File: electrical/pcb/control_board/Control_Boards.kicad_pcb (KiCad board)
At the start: 2 copper layers, 111 parts, among them J1 XT30-M, J10 Molex_172675-0613, J11 Molex_172675-0613, J12 TSW-104-07-F-T, J13 Molex_172675-0613, J14 Molex_172675-0613, J15 TSW-104-07-F-T, J16 ED2627-ND, J17 ED2627-ND, J18 ED2627-ND, J19 TSW-104-07-F-T, J2 XT30-F, J20 PEC08SAAN, J21 PPTC102LFBN-RC, J22 S9175-ND_rpi_breakout, J23 S9175-ND_rpi_breakout, J24 6posheader, J25 SSW-104-01-F-T, J26 PEC10DAAN, J27 PPTC021LFBN-RC, J28 PPTC021LFBN-RC, J29 PPTC021LFBN-RC, J3 XT30-F, J4 XT30-F, J5 XT30-M, J6 ED2580-ND, J7 TSW-104-07-F-T, J8 Molex_172675-0613, J9 Molex_172675-0613, M1 Mounting_Holes, Q1 2N3906, Q2 2N3906, Q3 2N3906, SW1 CT206124-ND, T1 test_point, T2 test_point, T3 test_point, T4 test_point, T5 test_point, T6 test_point, U1 INA260, U2 PCA9685, U3 D24V22Fx, U4 D24V150Fx, U5 DC7G3HWA, U6 DC7G3HWA, y1 rover_silkscreen

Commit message: Adding edge cuts to control boards
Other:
- board outline added: 181.6 x 252.8 mm

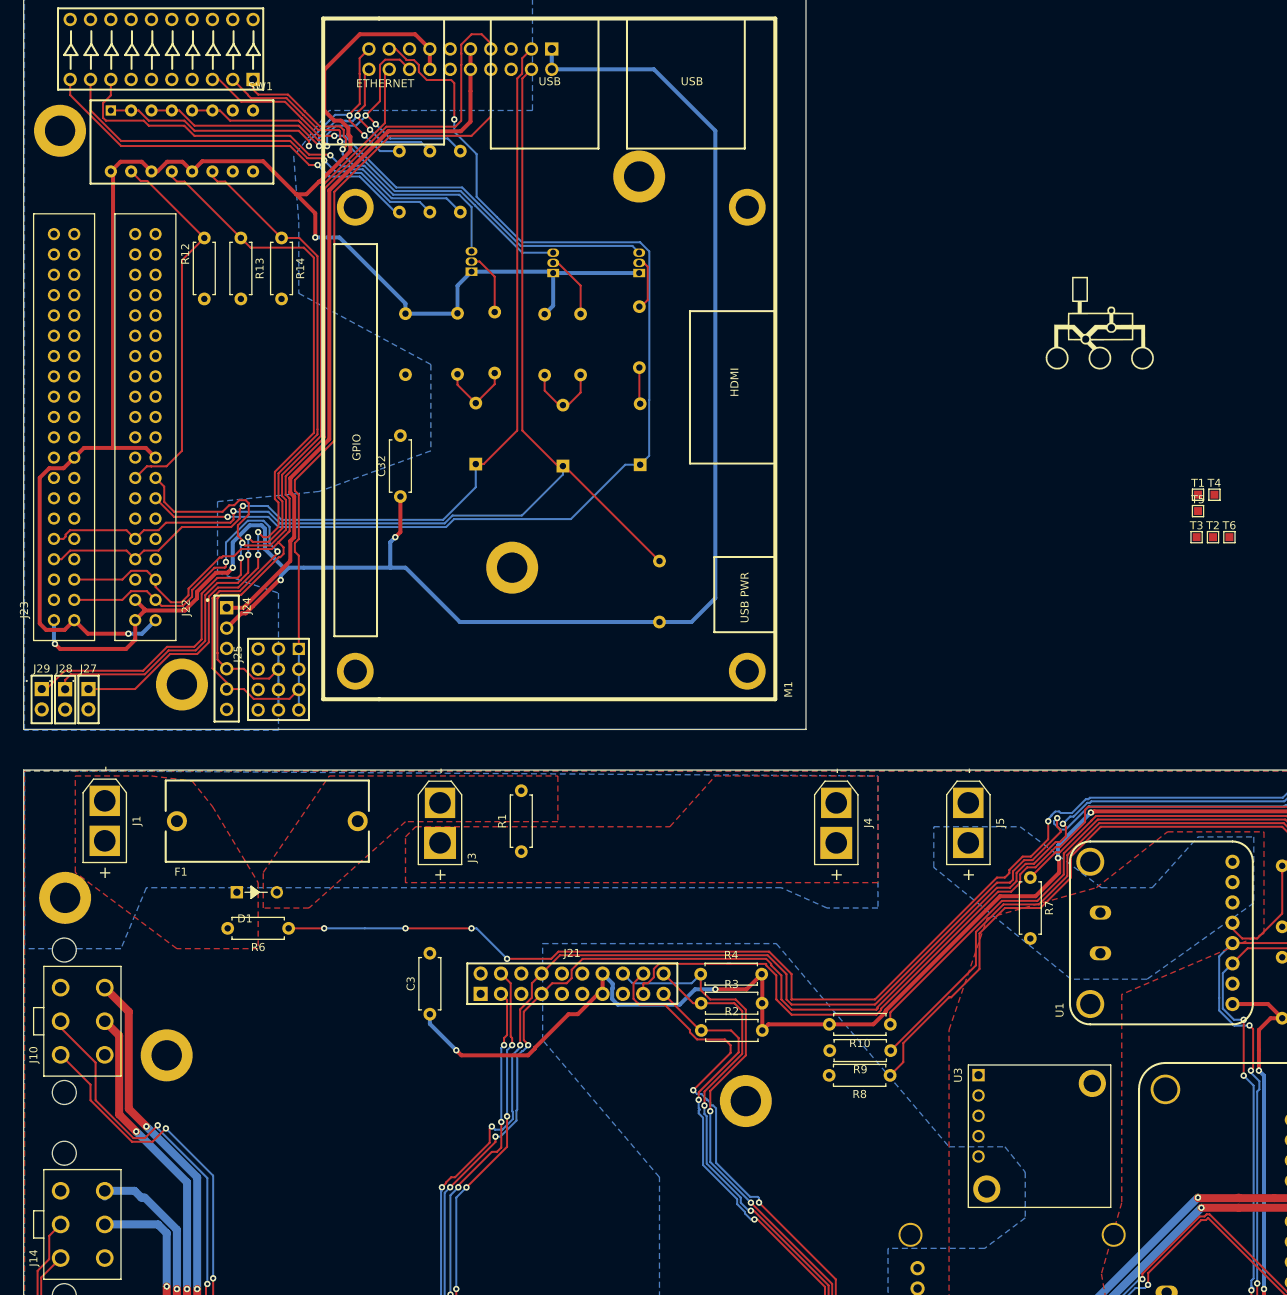
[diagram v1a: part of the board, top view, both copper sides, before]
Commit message: Updates to layout
- Placed 12V_enable line in layout
- Placed additional LED resistors in layout
- Placed testpoints in layout
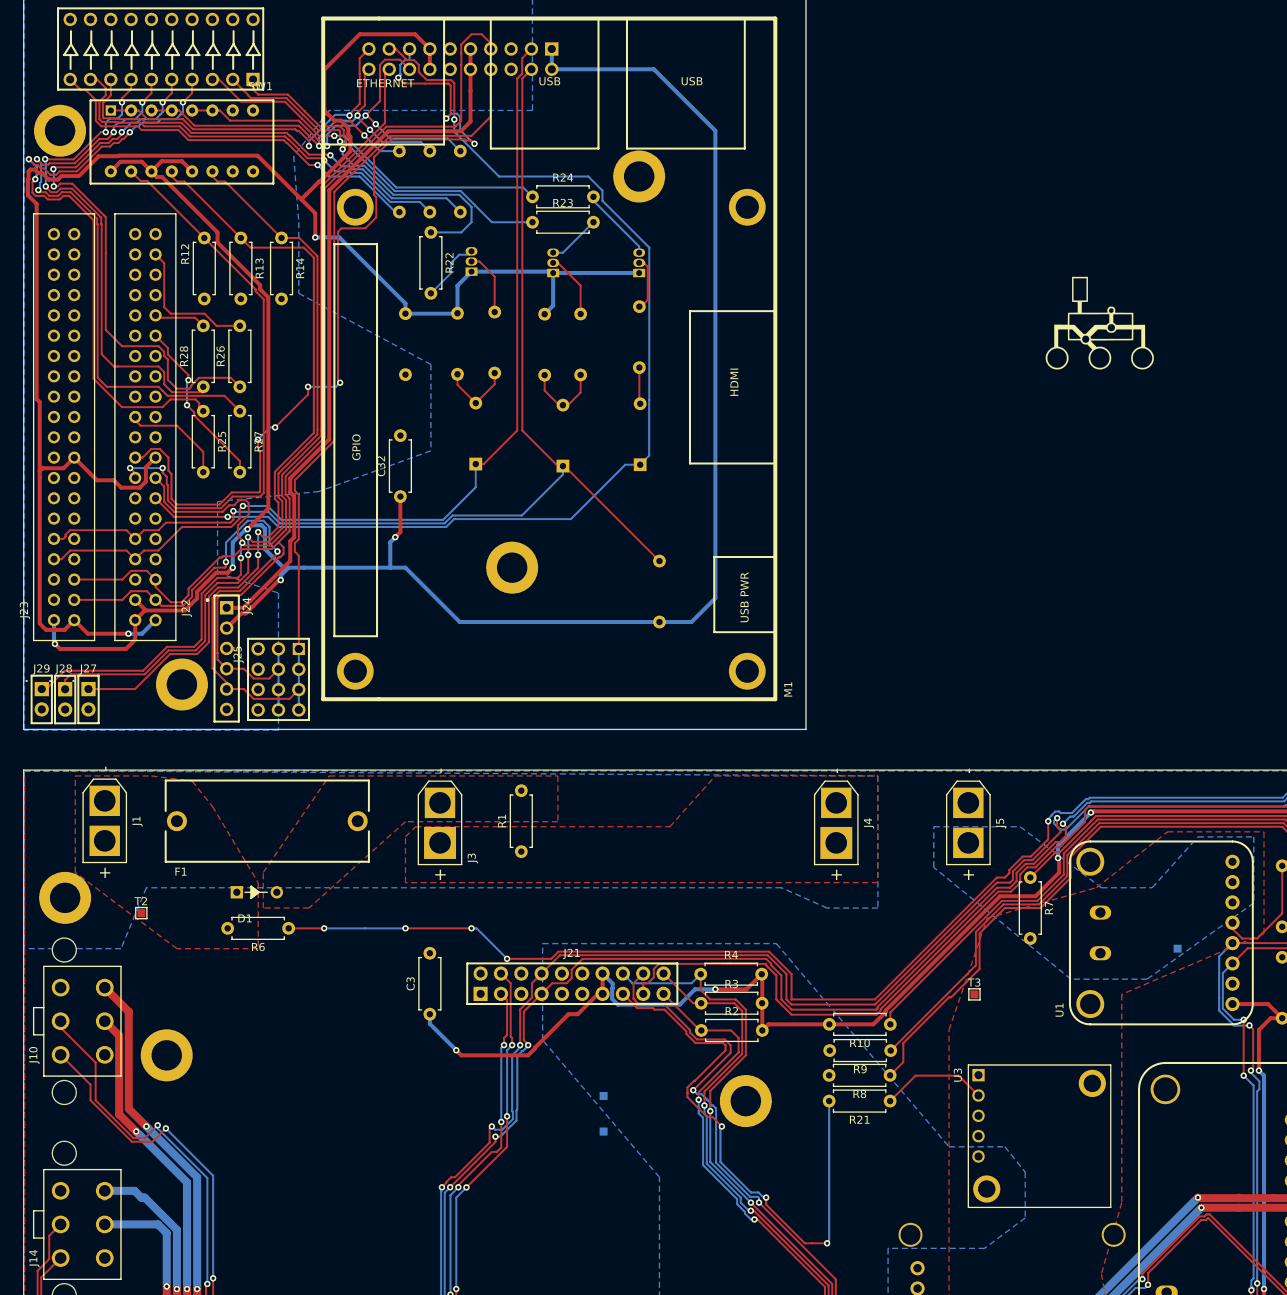
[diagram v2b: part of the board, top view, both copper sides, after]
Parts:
- removed T6: test_point, TestPoint:TestPoint_Pad_1.0x1.0mm
- added R21: 0, Resistor_THT:R_Axial_DIN0207_L6.3mm_D2.5mm_P7.62mm_Horizontal, F.Cu at (108.2, -114.9)
- added R22: 82, Resistor_THT:R_Axial_DIN0207_L6.3mm_D2.5mm_P7.62mm_Horizontal, F.Cu at (50.8, -223.5)
- added R23: 82, Resistor_THT:R_Axial_DIN0207_L6.3mm_D2.5mm_P7.62mm_Horizontal, F.Cu at (63.5, -224.8)
- added R24: 82, Resistor_THT:R_Axial_DIN0207_L6.3mm_D2.5mm_P7.62mm_Horizontal, F.Cu at (63.5, -228.0)
- added R25: 82, Resistor_THT:R_Axial_DIN0207_L6.3mm_D2.5mm_P7.62mm_Horizontal, F.Cu at (22.4, -201.2)
- added R26: 82, Resistor_THT:R_Axial_DIN0207_L6.3mm_D2.5mm_P7.62mm_Horizontal, F.Cu at (26.9, -204.2)
- added R27: 82, Resistor_THT:R_Axial_DIN0207_L6.3mm_D2.5mm_P7.62mm_Horizontal, F.Cu at (26.9, -201.2)
- added R28: 82, Resistor_THT:R_Axial_DIN0207_L6.3mm_D2.5mm_P7.62mm_Horizontal, F.Cu at (22.4, -204.2)
- R18, R19, R20: value 150 -> 200
- T1, T4, T5: moved to B.Cu
- moved T2 142.0 mm to (14.6, -138.4)
- moved T1 108.9 mm to (72.4, -111.1)
- moved T5 104.2 mm to (72.4, -115.6)
- moved T3 63.5 mm to (118.7, -128.3)
- moved T4 56.9 mm to (144.1, -134.0)
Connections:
- J21 pad 15: Net-(J21-Pad15) -> /Motor Board/12V_EN
- J22 pad 18: Net-(J22-Pad18) -> /Brain Board/12V_EN
- J22 pad 22: Net-(J22-Pad22) -> /Brain Board/RPI_LED_1
- J22 pad 29: Net-(J22-Pad29) -> /Brain Board/RPI_LED_3
- J22 pad 31: Net-(J22-Pad31) -> /Brain Board/RPI_LED_4
- J22 pad 37: Net-(J22-Pad37) -> /Brain Board/RPI_LED_2
- J26 pad 15: Net-(J26-Pad15) -> /Brain Board/12V_EN
- Q1 pad 3: /Brain Board/ALERT_LED -> Net-(Q1-Pad3)
- Q2 pad 3: /Brain Board/TXD_LED -> Net-(Q2-Pad3)
- Q3 pad 3: /Brain Board/RXD_LED -> Net-(Q3-Pad3)
- SW1 pad 10: +3.3V_brain -> +5V_brain
- SW1 pad 2: +3.3V_brain -> +5V_brain
- SW1 pad 6: +3.3V_brain -> +5V_brain
- T5 pad 1: GND_motor -> +12V_motor
- U3 pad 2: /Motor Board/12V_EN -> Net-(R21-Pad1)
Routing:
- net /Brain Board/12V_EN: track 0.00 -> 110.9 mm, vias 0 -> 7
- net Net-(R25-Pad1): track 0.00 -> 78.6 mm, vias 0 -> 4
- net Net-(R27-Pad1): track 0.00 -> 74.1 mm, vias 0 -> 4
- net /Motor Board/12V_EN: track 0.00 -> 70.5 mm, vias 0 -> 3
- net Net-(R26-Pad1): track 0.00 -> 68.7 mm, vias 0 -> 4
- net +5V_brain: track 210.8 -> 275.6 mm, vias 4 -> 5
- net Net-(R28-Pad1): track 0.00 -> 63.2 mm, vias 0 -> 4
- net /Brain Board/E_STOP_pi: track 47.6 -> 70.6 mm, vias 0 -> 2
- net /Brain Board/RPI_LED_3: track 0.00 -> 21.6 mm, vias 0 -> 2
- net /Brain Board/RPI_LED_2: track 0.00 -> 17.5 mm
- net +3.3V_brain: track 214.3 -> 230.9 mm
- net /Brain Board/ALERT_LED: track 62.3 -> 46.1 mm
- net Net-(R21-Pad1): track 0.00 -> 13.4 mm
- net /Brain Board/RPI_LED_1: track 0.00 -> 13.1 mm
- net Net-(Q1-Pad3): track 0.00 -> 9.35 mm
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
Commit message: Change solder mask clearance and min width to 0
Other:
- rule pad_to_mask_clearance: 0.051 -> 0

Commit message: Add 277-11404-ND
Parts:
- J16, J17, J18: value ED2627-ND -> 277-11404-ND

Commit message: Update PEC10DAAN to WM6548-ND
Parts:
- J26: value PEC10DAAN -> WM6548-ND
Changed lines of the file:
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@@
       (effects (font (size 1 1) (thickness 0.15)) (justify mirror))
     )
-    (fp_text value PEC10DAAN (at 3.048 2.54 180) (layer B.Fab)
+    (fp_text value WM6548-ND (at 3.048 2.54 180) (layer B.Fab)
       (effects (font (size 1 1) (thickness 0.15)) (justify mirror))
     )

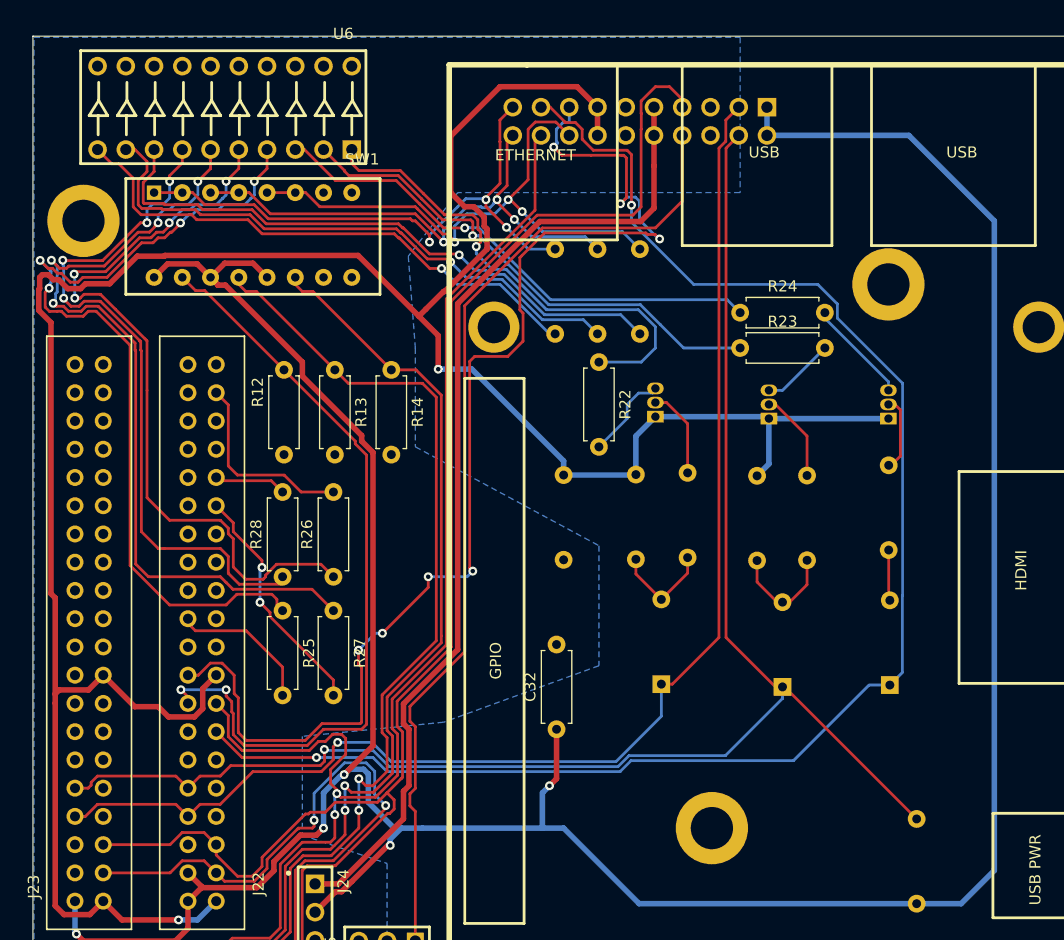
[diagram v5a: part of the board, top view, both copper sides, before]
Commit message: Fixing incorrect orientation of inter board connector on brain board
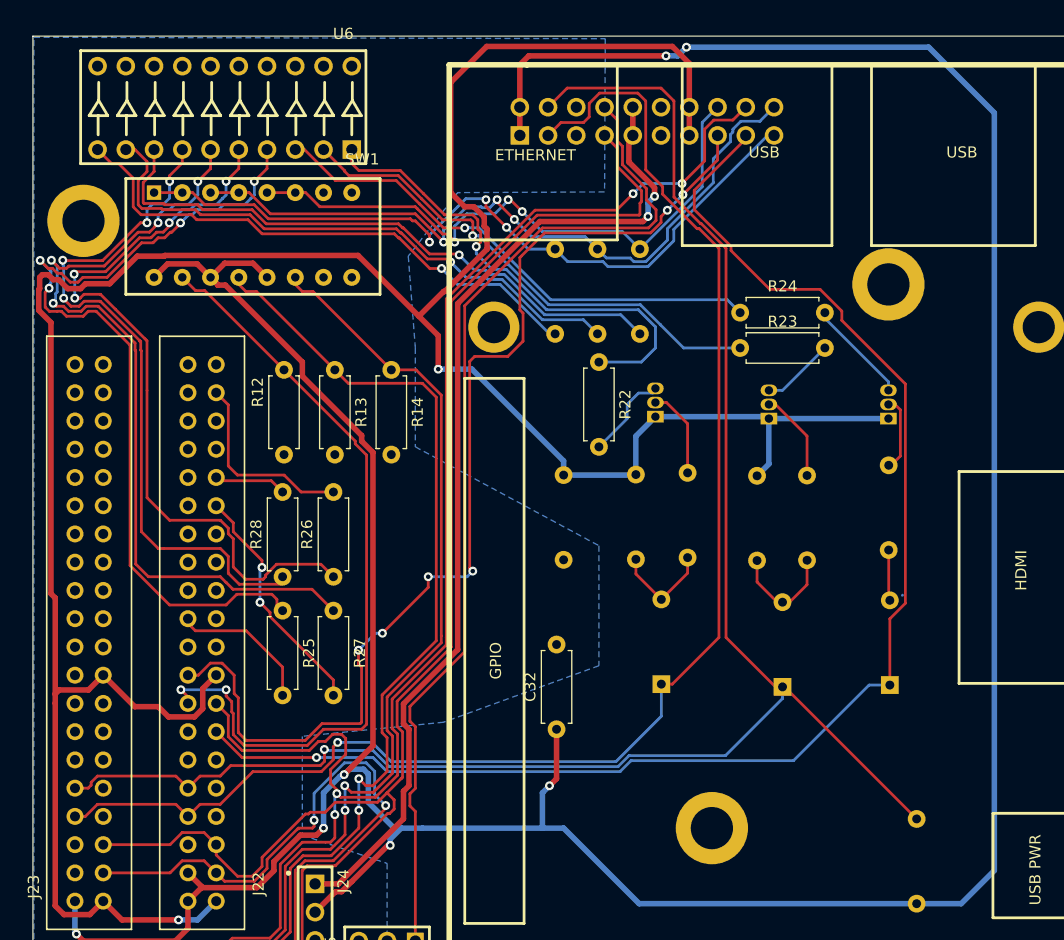
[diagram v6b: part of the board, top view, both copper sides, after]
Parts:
- moved J26 22.4 mm to (43.7, -243.9), turned to 0 degrees
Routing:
- net +5V_brain: track 275.6 -> 311.5 mm, vias 5 -> 7
- net /Brain Board/E_STOP2: track 47.5 -> 65.4 mm
- net /Brain Board/OEservos: track 129.1 -> 146.7 mm, vias 2 -> 4
- net /Brain Board/RXD: track 140.5 -> 157.6 mm
- net /Brain Board/E_STOP: track 51.9 -> 68.5 mm
- net +3.3V_brain: track 230.9 -> 247.3 mm
- net /Brain Board/TXD: track 117.7 -> 131.7 mm
- net /Brain Board/alert: track 140.6 -> 127.8 mm, vias 2 -> 1
- net /Brain Board/12V_EN: track 110.9 -> 98.9 mm, vias 7 -> 6
- net /Brain Board/SCL_rpi: track 150.9 -> 144.2 mm
- net /Brain Board/E_STOP3: track 51.3 -> 55.4 mm
- net /Brain Board/SDA_rpi: track 165.7 -> 168.8 mm
- net +12V_brain: track 89.4 -> 90.7 mm, vias 0 -> 2

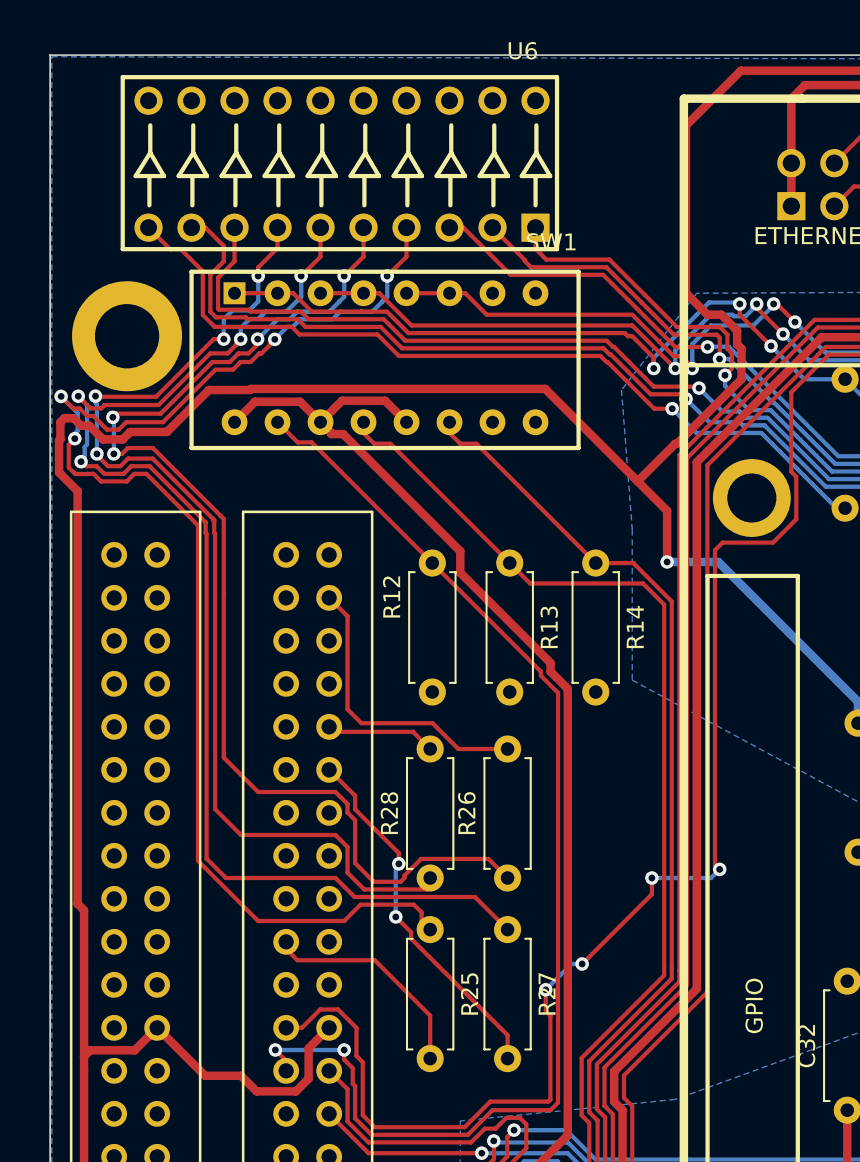
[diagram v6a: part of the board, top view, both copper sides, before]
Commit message: Updated footprint for LED block. Partial re-route on brain board for updated LED footprint
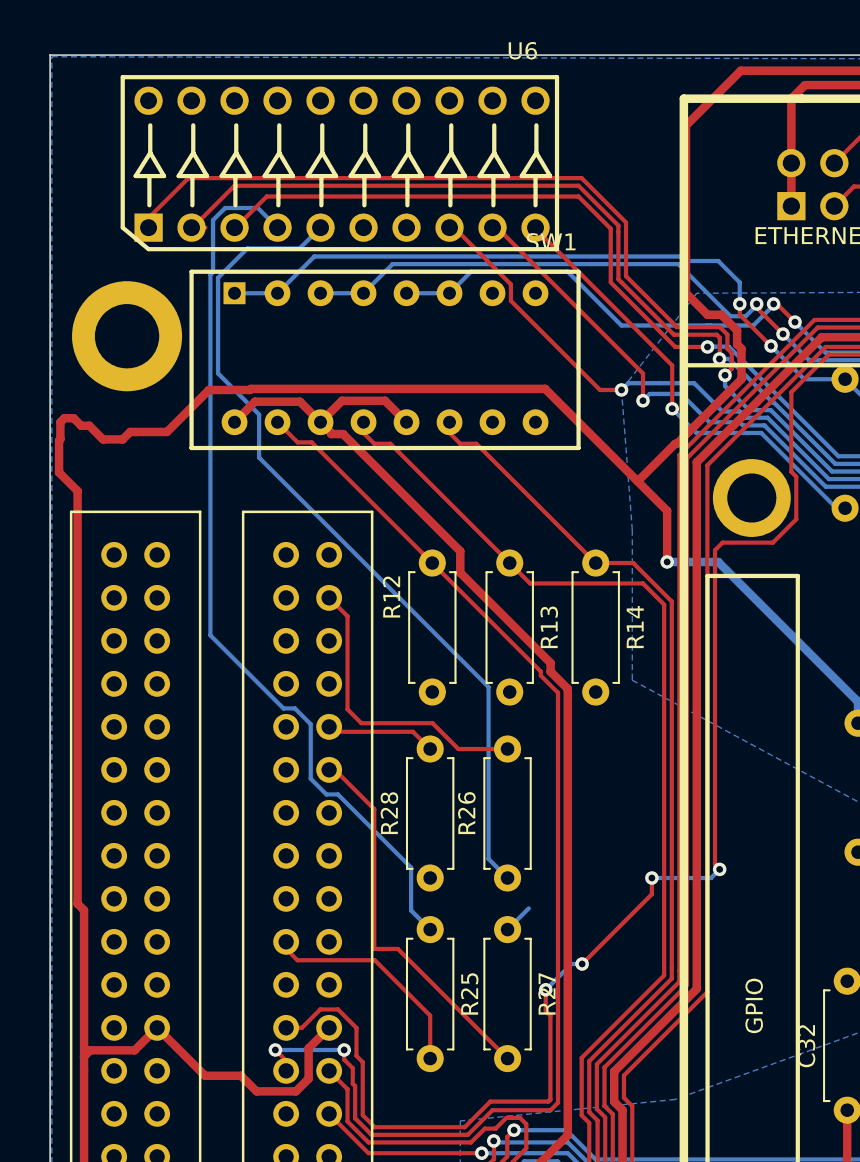
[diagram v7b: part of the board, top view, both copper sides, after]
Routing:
- net Net-(R27-Pad1): track 74.1 -> 1.77 mm, vias 4 -> 0
- net Net-(R28-Pad1): track 63.2 -> 1.08 mm, vias 4 -> 0
- net /Brain Board/TXD_LED: track 44.3 -> 71.1 mm
- net Net-(R25-Pad1): track 78.6 -> 53.3 mm, vias 4 -> 0
- net /Brain Board/ESTOP_LED_1: track 49.5 -> 26.6 mm
- net /Brain Board/RXD_LED: track 45.7 -> 68.2 mm
- net /Brain Board/ESTOP_LED_2: track 52.7 -> 32.8 mm
- net Net-(R26-Pad1): track 68.7 -> 49.5 mm, vias 4 -> 0
- net /Brain Board/ALERT_LED: track 46.1 -> 62.2 mm
- net /Brain Board/ESTOP_LED_3: track 54.7 -> 38.7 mm
- net /Brain Board/E_STOP3: track 55.4 -> 53.4 mm, vias 3 -> 2
- net /Brain Board/E_STOP2: track 65.4 -> 63.6 mm, vias 3 -> 2
- net /Brain Board/E_STOP: track 68.5 -> 67.2 mm, vias 3 -> 2
- net /Brain Board/RPI_LED_3: track 21.6 -> 22.4 mm, vias 2 -> 0
